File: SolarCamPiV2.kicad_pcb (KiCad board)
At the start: 2 copper layers, 65 x 30 mm, 68 parts, among them Q1 AO3401A, Q2 AO3401A, Q3 2N7002, Q4 AO3401A, Q5 2N7002, Q6 BSS84, SW1 SW_Push, U1 CN3767, U2 HT7533, U3 SY8113B

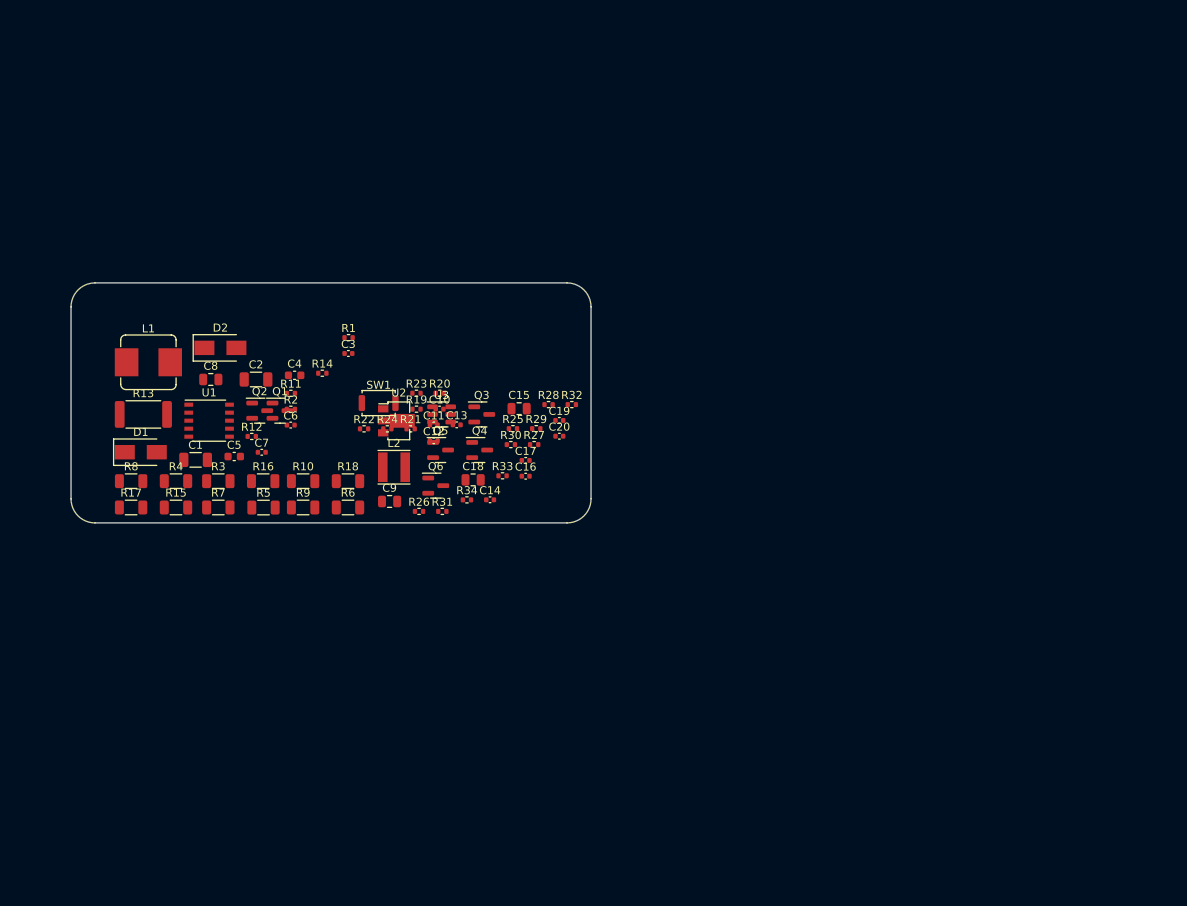
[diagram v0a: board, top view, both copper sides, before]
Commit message: Add reverse polarity protection
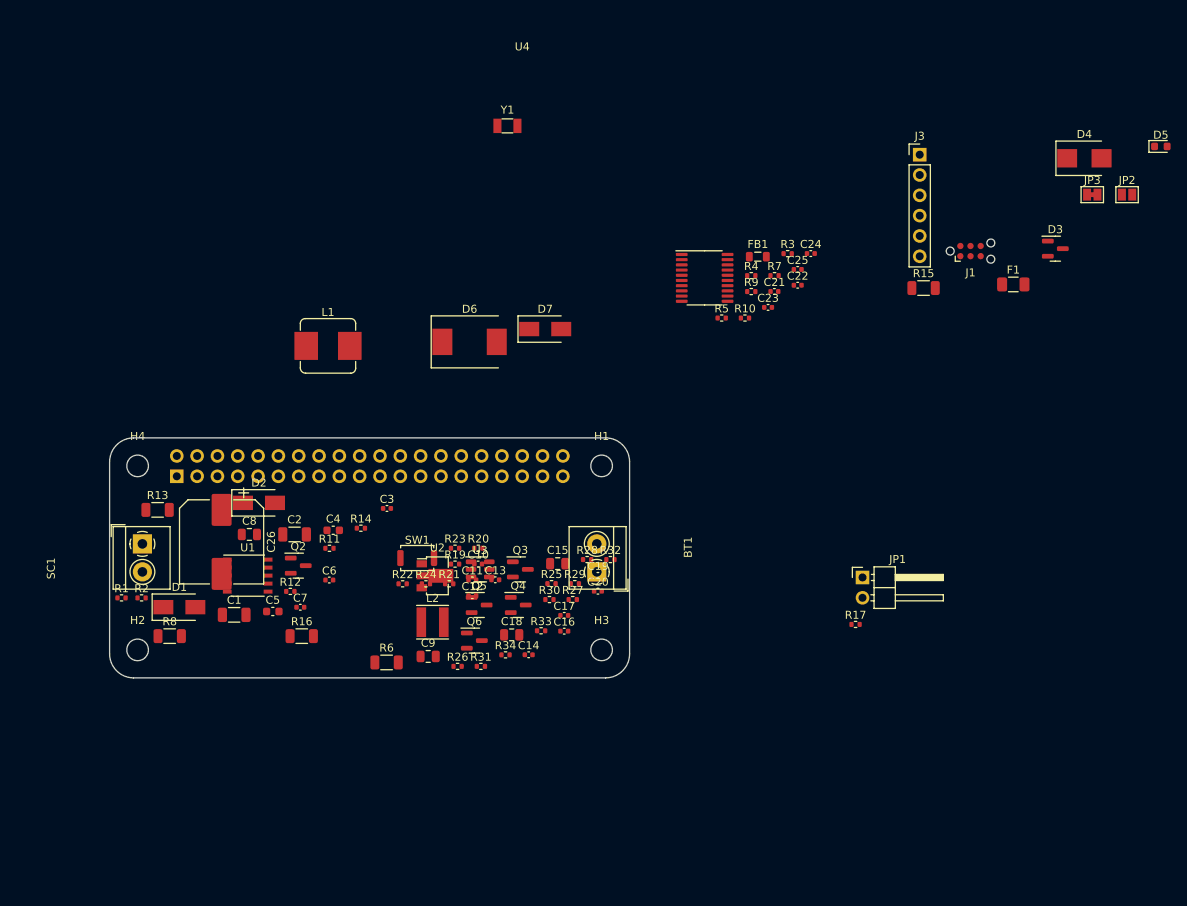
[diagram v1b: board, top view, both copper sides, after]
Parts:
- removed Q1: AO3401A, Package_TO_SOT_SMD:SOT-23
- removed R18: 0.1R, Resistor_SMD:R_1206_3216Metric
- added BT1: Battery, TerminalBlock_4Ucon:TerminalBlock_4Ucon_1x02_P3.50mm_Horizontal, F.Cu at (160.9, 116.8)
- added C21: 100nF, Capacitor_SMD:C_0402_1005Metric, F.Cu at (183.1, 81.7)
- added C22: 22pF, Capacitor_SMD:C_0402_1005Metric, F.Cu at (186.0, 80.9)
- added C23: 22pF, Capacitor_SMD:C_0402_1005Metric, F.Cu at (182.3, 83.7)
- added C24: 1uF, Capacitor_SMD:C_0402_1005Metric, F.Cu at (187.7, 77.0)
- added C25: 100nF, Capacitor_SMD:C_0402_1005Metric, F.Cu at (186.0, 79.0)
- added C26: 220uF 35V, Capacitor_SMD:CP_Elec_10x10, F.Cu at (114.0, 113.0)
- added D3: BAV70, Package_TO_SOT_SMD:SOT-23, F.Cu at (218.2, 76.3)
- added D4: 6.8CA, Diode_SMD:D_SMB, F.Cu at (221.8, 65.0)
- added D5: PWR, LED_SMD:LED_0603_1608Metric, F.Cu at (231.4, 63.6)
- added D6: SS36, Diode_SMD:D_SMC, F.Cu at (145.0, 88.0)
- added D7: M7, Diode_SMD:D_SMA, F.Cu at (154.4, 86.4)
- added F1: 2A, Fuse:Fuse_1206_3216Metric, F.Cu at (213.0, 80.8)
- added FB1: 100R@100MHz, Inductor_SMD:L_0805_2012Metric, F.Cu at (181.0, 77.3)
- added H1: MountingHole, MountingHole:MountingHole_2.7mm_M2.5, F.Cu at (161.5, 103.5)
- added H2: MountingHole, MountingHole:MountingHole_2.7mm_M2.5, F.Cu at (103.5, 126.5)
- added H3: MountingHole, MountingHole:MountingHole_2.7mm_M2.5, F.Cu at (161.5, 126.5)
- added H4: MountingHole, MountingHole:MountingHole_2.7mm_M2.5, F.Cu at (103.5, 103.5)
- added J1: TagConnect_TC2030_SWD, Connector:Tag-Connect_TC2030-IDC-NL_2x03_P1.27mm_Vertical, F.Cu at (207.6, 76.7)
- added J2: RPi, Connector_PinSocket_2.54mm:PinSocket_2x20_P2.54mm_Vertical, B.Cu at (108.4, 104.8)
- added J3: FTDI_RPI, Connector_PinHeader_2.54mm:PinHeader_1x06_P2.54mm_Vertical, F.Cu at (201.3, 64.6)
- added JP1: Force on, Connector_PinHeader_2.54mm:PinHeader_1x02_P2.54mm_Horizontal, F.Cu at (194.1, 117.5)
- added JP2: Pi -> STM RST, Jumper:SolderJumper-2_P1.3mm_Open_Pad1.0x1.5mm, F.Cu at (227.2, 69.6)
- added JP3: Pi -> PWR ON, Jumper:SolderJumper-2_P1.3mm_Bridged_Pad1.0x1.5mm, F.Cu at (222.8, 69.6)
- added SC1: Solar_Cells, TerminalBlock_4Ucon:TerminalBlock_4Ucon_1x02_P3.50mm_Horizontal, F.Cu at (104.1, 113.2)
- added U4: STM32G031Fx, Package_SO:TSSOP-20_4.4x6.5mm_P0.65mm, F.Cu at (174.4, 80.0)
- added Y1: 32.768kHz, Crystal:Crystal_SMD_3215-2Pin_3.2x1.5mm, F.Cu at (149.7, 61.0)
- R10: value 0.1R -> 100R; footprint Resistor_SMD:R_1206_3216Metric -> Resistor_SMD:R_0402_1005Metric
- R13: value 10mR -> 1R; footprint Resistor_SMD:R_2512_6332Metric -> Resistor_SMD:R_1206_3216Metric
- R17: value 0.1R -> 15k; footprint Resistor_SMD:R_1206_3216Metric -> Resistor_SMD:R_0402_1005Metric
- R3, R4, R7, R9: value 0.1R -> 100k; footprint Resistor_SMD:R_1206_3216Metric -> Resistor_SMD:R_0402_1005Metric
- R5: value 0.1R -> 10k; footprint Resistor_SMD:R_1206_3216Metric -> Resistor_SMD:R_0402_1005Metric
- SW1: value SW_Push -> User
- moved R15 97.4 mm to (201.7, 81.3)
- moved R17 91.7 mm to (193.2, 123.3)
- moved R3 76.6 mm to (184.8, 77.0)
- moved R4 76.4 mm to (180.2, 79.7)
- moved R7 75.3 mm to (183.1, 79.7)
- moved R9 62.2 mm to (180.2, 81.7)
- moved R5 62.0 mm to (176.5, 85.0)
- moved R10 58.9 mm to (179.4, 85.0)
- moved R1 43.2 mm to (101.5, 120.0)
- moved R2 30.1 mm to (104.0, 120.0)
- moved L1 22.5 mm to (127.3, 88.5)
- moved C15 20.0 mm to (156.0, 115.7)
- moved C17 20.0 mm to (156.8, 122.2)
- moved C19 20.0 mm to (161.0, 117.2)
- moved R25 20.0 mm to (155.2, 118.2)
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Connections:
- net /I_charge renamed /I_{Charge}
- net /I_load renamed /I_{Load}
- net /I_solar renamed /I_{Solar}
- net /U_solar renamed /U_{Solar}
- net /rpi_on renamed Net-(Q3-Pad1)
- C1 pad 2: Net-(C1-Pad2) -> /+SOLAR
- C14 pad 2: Net-(C14-Pad2) -> +BATT
- C18 pad 1: Net-(C18-Pad1) -> +5V
- C19 pad 1: Net-(C18-Pad1) -> +5V
- C2 pad 2: Net-(C1-Pad2) -> /+SOLAR
- C20 pad 1: GND -> /U_{Batt}
- C20 pad 2: /U_batt -> GND
- C4 pad 1: Net-(C1-Pad2) -> /+SOLAR
- C5 pad 1: Net-(C1-Pad2) -> /+SOLAR
- C8 pad 2: Net-(C8-Pad2) -> +BATT
- C9 pad 2: Net-(C8-Pad2) -> +BATT
- L2 pad 2: Net-(C18-Pad1) -> +5V
- Q2 pad 3: Net-(C1-Pad2) -> /+SOLAR
- Q4 pad 2: Net-(Q4-Pad2) -> +BATT
- Q6 pad 2: unconnected-(Q6-Pad2) -> +BATT
- R1 pad 1: Net-(C1-Pad2) -> /+SOLAR
- R10 pad 1: GND2 -> Net-(R7-Pad1)
- R10 pad 2: Net-(R10-Pad2) -> /U_{Load}
- R13 pad 1: Net-(L1-Pad2) -> /+SOLAR
- R13 pad 2: Net-(C8-Pad2) -> Net-(C26-Pad1)
- R14 pad 1: Net-(C8-Pad2) -> +BATT
- R15 pad 1: GND2 -> Net-(L1-Pad2)
- R15 pad 2: Net-(R15-Pad2) -> +BATT
- R16 pad 1: Net-(R16-Pad1) -> GND3
- R17 pad 1: Net-(R15-Pad2) -> +5V
- R17 pad 2: GND3 -> Net-(D5-Pad2)
- R19 pad 1: Net-(C1-Pad2) -> /+SOLAR
- R25 pad 2: Net-(Q4-Pad2) -> +BATT
- R27 pad 1: Net-(C18-Pad1) -> +5V
- R3 pad 1: GND -> +3V3
- R3 pad 2: Net-(R3-Pad2) -> /~{DONE}
- R31 pad 2: Net-(Q6-Pad3) -> +BATT
- R34 pad 1: Net-(R32-Pad2) -> /U_{Batt}
- R34 pad 2: /U_batt -> Net-(R32-Pad2)
- R4 pad 1: Net-(R4-Pad1) -> /~{CHRG}
- R4 pad 2: GND -> +3V3
- R5 pad 1: Net-(R3-Pad2) -> +3V3
- R5 pad 2: GND1 -> /~{RST}
- R6 pad 2: Net-(R4-Pad1) -> GND
- R7 pad 1: GND1 -> Net-(R7-Pad1)
- R7 pad 2: Net-(R7-Pad2) -> +5V
- R8 pad 1: Net-(R10-Pad2) -> GND2
- R9 pad 1: Net-(R7-Pad2) -> GND
- R9 pad 2: GND2 -> Net-(R7-Pad1)
- SW1 pad 1: unconnected-(SW1-Pad1) -> +3V3
- SW1 pad 2: unconnected-(SW1-Pad2) -> /u_batt_div_on
- U1 pad 9: Net-(C1-Pad2) -> /+SOLAR
- U2 pad 2: Net-(C14-Pad2) -> +BATT

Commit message: Layout power conversion subcomponents
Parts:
- added Q1: AO3401A, Package_TO_SOT_SMD:SOT-23, F.Cu at (132.6, 108.5)
- moved C10 79.6 mm to (224.2, 100.9)
- moved C11 79.6 mm to (223.5, 102.9)
- moved C12 79.6 mm to (223.5, 104.9)
- moved C13 79.6 mm to (226.4, 102.9)
- moved R23 79.6 mm to (221.3, 98.9)
- moved R24 79.6 mm to (217.7, 103.4)
- moved SW1 79.6 mm to (216.6, 100.2)
- moved R15 75.6 mm to (132.9, 112.5), turned to -90 degrees
- moved F1 67.8 mm to (154.4, 115.0), turned to 180 degrees
- moved R26 66.8 mm to (205.7, 104.1)
- moved R16 66.7 mm to (183.9, 154.2)
- moved R3 64.1 mm to (130.2, 110.7), turned to 180 degrees
- moved L2 61.5 mm to (198.2, 102.0), turned to 180 degrees
- moved R4 60.9 mm to (127.8, 110.7)
- moved Q3 56.2 mm to (205.6, 101.7), turned to 90 degrees
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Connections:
- Q2 pad 2: Net-(D1-Pad2) -> /+SOLAR
- Q2 pad 3: /+SOLAR -> Net-(D1-Pad2)
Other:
- copper layers 2 -> 4

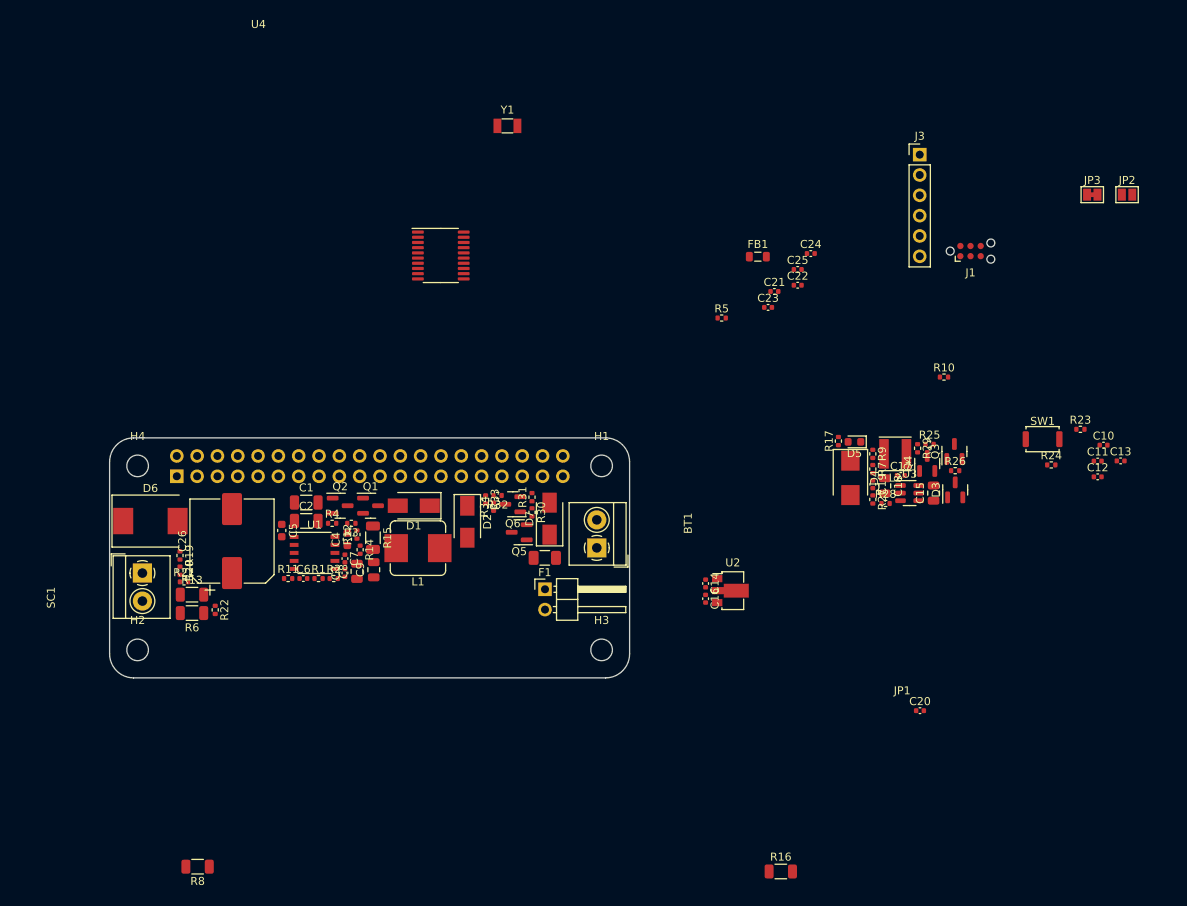
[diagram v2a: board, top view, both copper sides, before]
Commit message: Finish component placement
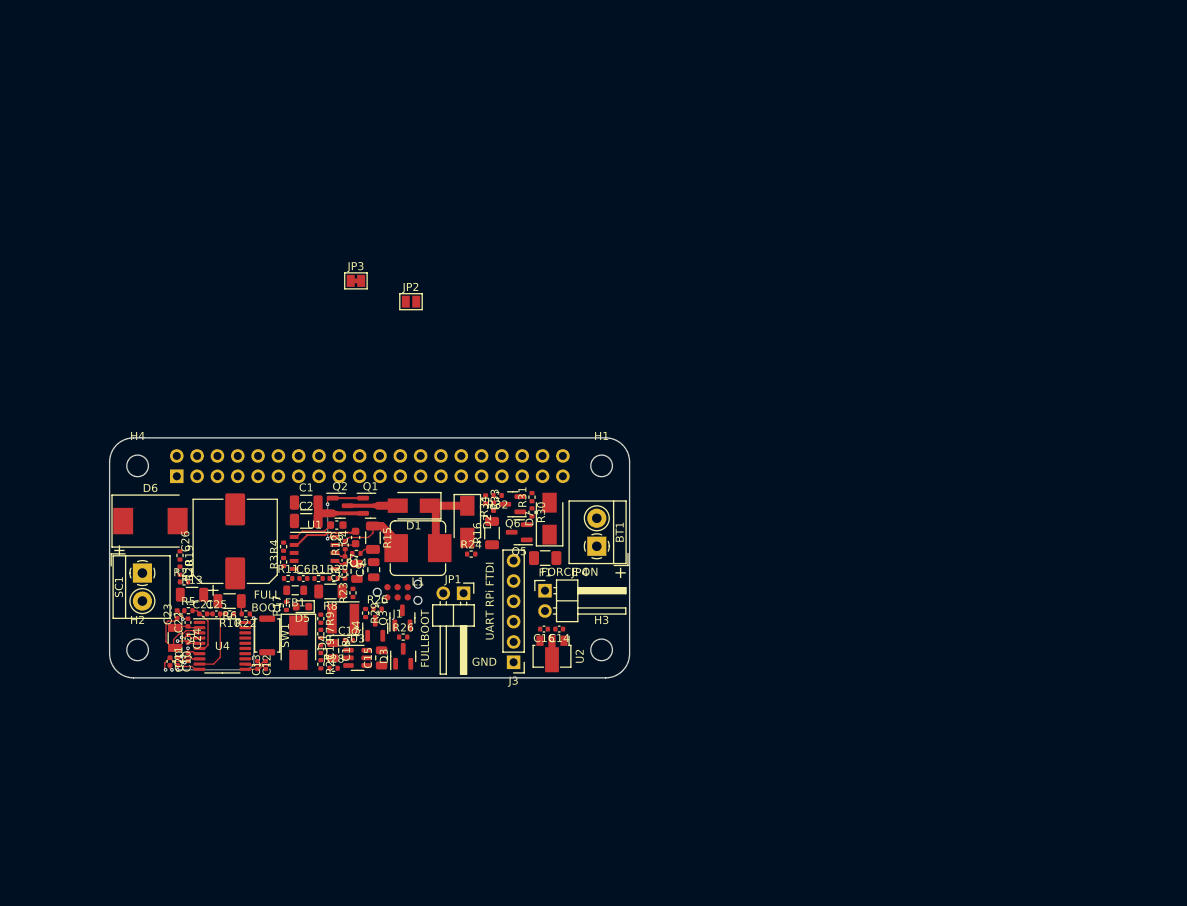
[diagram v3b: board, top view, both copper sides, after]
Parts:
- added JP4: User, Connector_PinHeader_2.54mm:PinHeader_1x02_P2.54mm_Horizontal, F.Cu at (154.4, 119.1)
- moved C10 118.9 mm to (108.5, 128.0), turned to -90 degrees
- moved C11 116.3 mm to (109.8, 127.4), turned to 90 degrees
- moved C13 109.9 mm to (119.5, 128.4), turned to 90 degrees
- moved C12 107.6 mm to (118.5, 128.4), turned to -90 degrees
- moved SW1 100.0 mm to (119.7, 124.7), turned to -90 degrees
- moved R10 94.1 mm to (115.0, 122.0), turned to 180 degrees
- moved C20 94.0 mm to (107.5, 128.0), turned to -90 degrees
- moved R23 93.2 mm to (130.4, 119.4), turned to 90 degrees
- moved JP3 92.7 mm to (130.8, 80.4)
- moved C24 91.5 mm to (109.8, 125.1), turned to -90 degrees
- moved JP2 90.5 mm to (137.7, 83.0)
- moved C22 87.1 mm to (109.8, 123.1), turned to 90 degrees
- moved C25 84.5 mm to (113.3, 122.0)
- moved J1 83.4 mm to (136.0, 119.3)
- moved C23 83.2 mm to (108.5, 122.0), turned to 90 degrees
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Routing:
- net /I_{Solar}: track 0.00 -> 19.2 mm, vias 0 -> 2
- net /+SOLAR: track 0.00 -> 10.8 mm
- net Net-(D1-Pad1): track 0.00 -> 10.5 mm
- net Net-(Q1-Pad1): track 0.00 -> 10.4 mm, vias 0 -> 2
- net Net-(C23-Pad1): track 0.00 -> 10.0 mm
- net Net-(L1-Pad2): track 0.00 -> 9.36 mm
- net /U_{Load}: track 0.00 -> 9.07 mm
- net Net-(D1-Pad2): track 0.00 -> 8.70 mm
- net GND2: track 0.00 -> 8.39 mm
- net GND: track 0.00 -> 7.34 mm, vias 0 -> 5
- net /~{RST}: track 0.00 -> 7.25 mm
- net /U_{Batt}: track 0.00 -> 6.04 mm, vias 0 -> 1
- net Net-(C5-Pad2): track 0.00 -> 4.90 mm
- net /I_{Charge}: track 0.00 -> 3.35 mm
- net Net-(C22-Pad1): track 0.00 -> 3.14 mm
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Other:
- board text added: "+"
- board text added: "FORCE ON"
- board text added: "FULL BOOT"
- board text added: "FULLBOOT"
- board text added: "GND"
- board text added: "UART RPi FTDI"

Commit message: Finish routing
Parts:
- JP2, JP3: moved to B.Cu
- moved JP2 34.8 mm to (117.7, 111.5), turned to 90 degrees
- moved JP3 32.9 mm to (120.2, 111.5), turned to 90 degrees
- moved J1 1.18 mm to (137.2, 119.3)
- moved FB1 0.25 mm to (122.9, 119.0)
- moved R16 0.10 mm to (147.7, 111.9)
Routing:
- net /U_{Batt}: track 6.04 -> 66.4 mm, vias 1 -> 2
- net /u_batt_div_on: track 0.00 -> 59.8 mm, vias 0 -> 2
- net +BATT: track 1.78 -> 58.6 mm, vias 0 -> 21
- net GND2: track 8.39 -> 62.8 mm, vias 0 -> 23
- net /TX: track 0.00 -> 51.0 mm, vias 0 -> 1
- net /~{RST}: track 7.25 -> 56.0 mm, vias 0 -> 5
- net /RX: track 0.00 -> 48.4 mm
- net GND: track 7.34 -> 54.3 mm, vias 5 -> 34
- net /+SOLAR: track 10.8 -> 56.5 mm, vias 0 -> 18
- net /I_{Load}: track 2.83 -> 43.4 mm, vias 0 -> 2
- net /I_{Charge}: track 3.35 -> 40.3 mm, vias 0 -> 6
- net /rpi_on_stm: track 0.00 -> 34.0 mm, vias 0 -> 2
- net /rpi_on_rpi: track 0.00 -> 33.3 mm, vias 0 -> 1
- net GND3: track 0.00 -> 32.7 mm, vias 0 -> 11
- net /SWCLK: track 0.00 -> 30.2 mm, vias 0 -> 2
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- added copper zone on In2.Cu, net +3V3
- added copper zone on In2.Cu, net +5V
- added copper zone on In2.Cu, net +BATT
- added copper zone on B.Cu, net /+SOLAR
- added copper zone on In2.Cu, net /+SOLAR
- added copper zone on In1.Cu, net GND
- added copper zone on In2.Cu, net GND
- added copper zone on In1.Cu, net GND1
- added copper zone on In1.Cu, net GND2
- added copper zone on In1.Cu, net GND3
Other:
- board text added: "BATTERY"
- board text added: "JLCJLCJLCJLC"
- board text added: "POWER ON"
- board text added: "SOLAR"
- board text added: "STM ~{RST}"
- board text added: "SWD"
- board text added: "Solar Cam Pi V2 Rev 1.0 Designed by Tobias Schramm in 2022"
